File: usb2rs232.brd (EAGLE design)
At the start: 34 x 13.2 mm, 11 parts, among them U1 CP2101, U2 MAX232

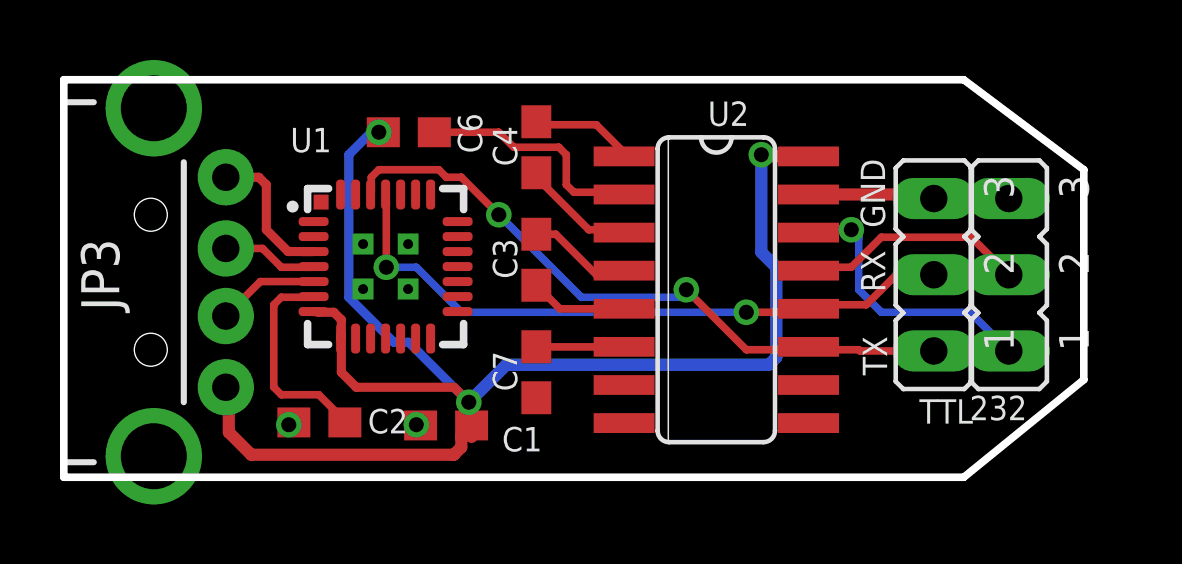
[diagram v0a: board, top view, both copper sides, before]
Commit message: Fix CP2102 package issues
Change-Id: I1545ad8a51535be1dc4a5aefa6ad10a204795dc0
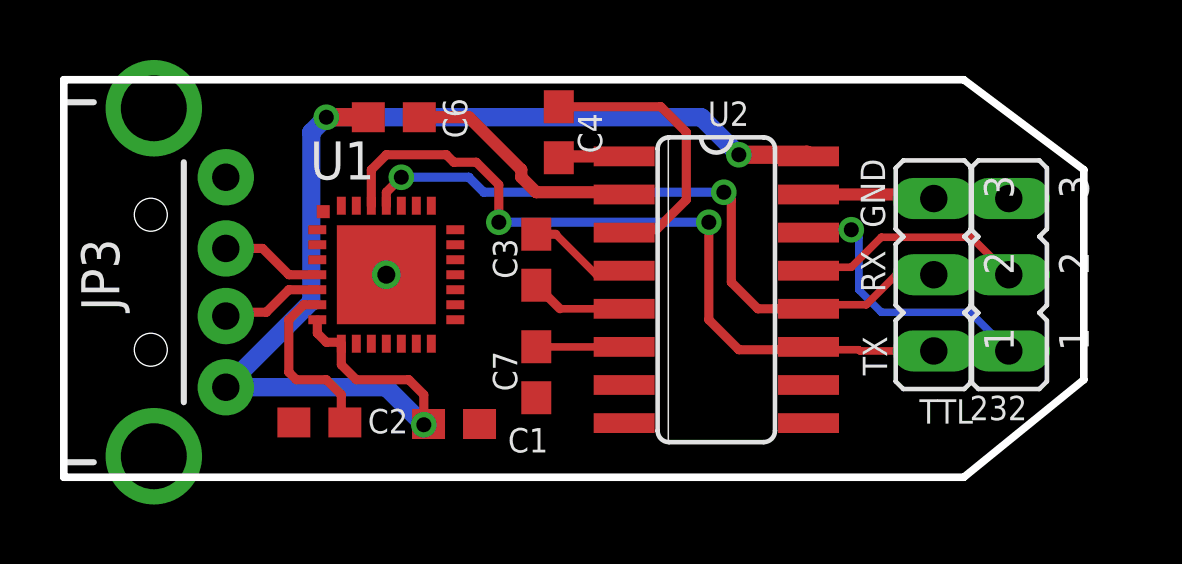
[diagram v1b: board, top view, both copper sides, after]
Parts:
- U1: value CP2101 -> CP2102; device futz:QFN-28 -> silabs:MLP28
- moved C4 0.90 mm to (16.0, 51.0), turned to 270 degrees
- moved C6 0.71 mm to (10.5, 51.5)
- moved U1 0.27 mm to (10.2, 46.2)
- moved C1 0.27 mm to (12.5, 41.3), turned to 180 degrees
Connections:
- net GND: now also U1.EXP, U1.M
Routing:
- net VCC: track 50.4 -> 42.2 mm
- net GND: track 12.5 -> 6.73 mm, vias 2 -> 1
- net N$4: track 3.84 -> 9.38 mm
- net N$2: track 22.2 -> 25.6 mm
- net N$3: track 3.48 -> 2.20 mm
- net N$16: track 21.8 -> 22.8 mm
- net N$15: track 7.08 -> 6.13 mm
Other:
- board text removed: "C1"
- board text removed: "C4"
- board text removed: "C6"
- board text removed: "U1"

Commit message: modify CP2012 for manual soldering
Change-Id: I582c1d6d425d662aba0cd10d8b75fda7aa71563e
Signed-off-by: Hasan Wan <hasan.wan@intel.com>
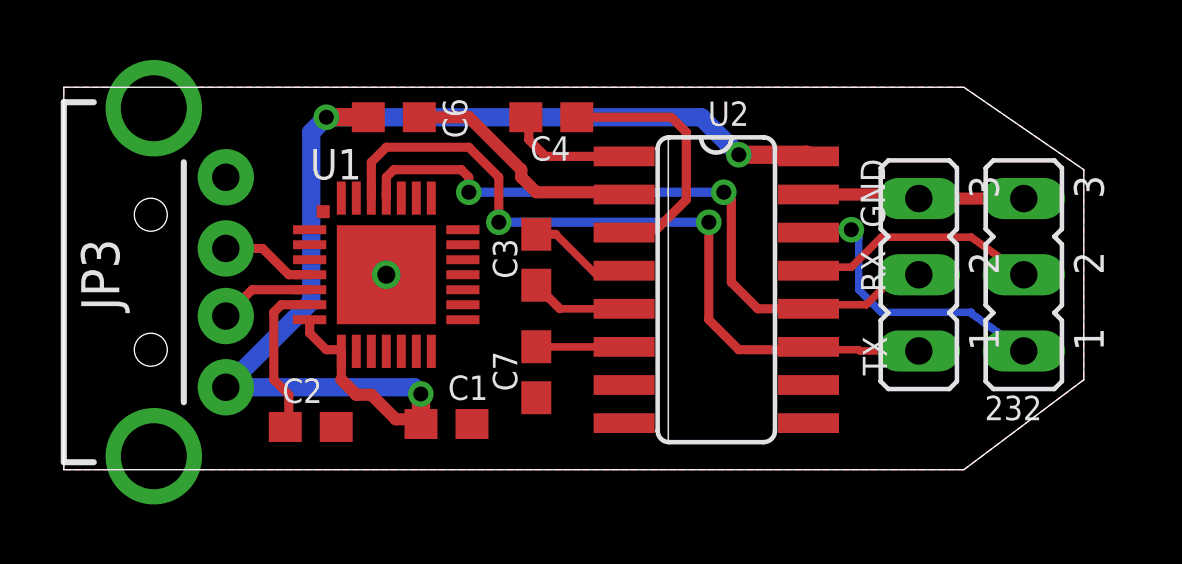
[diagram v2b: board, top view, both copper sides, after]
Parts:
- moved C4 0.56 mm to (15.8, 51.5), turned to 180 degrees
- moved 232 0.50 mm to (31.5, 46.2)
- moved TTL 0.50 mm to (28.0, 46.2)
- moved C2 0.32 mm to (7.73, 41.2), turned to 180 degrees
- moved C1 0.25 mm to (12.3, 41.3)
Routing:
- net N$3: track 2.20 -> 4.20 mm
- net GND: track 6.73 -> 7.93 mm
- net N$15: track 6.13 -> 5.38 mm
- net N$4: track 9.38 -> 8.63 mm
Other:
- board size 34 x 13.2 mm -> 34 x 12.8 mm
- board text added: "C1"
- board text added: "C4"
- board text added: "C6"
- board text added: "U1"
- board text removed: "TTL"
